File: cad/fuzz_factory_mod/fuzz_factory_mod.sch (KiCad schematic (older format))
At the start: 2 parts

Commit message: Continued schematic.
Modified fuuz_factory circuit : use of matched transistor pairs.
Added USB interface, through FT230X and direct to MCU.
Associated footprints, except for XTAL and trimmers.
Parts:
- NT101, NT102: renamed from NT?; footprint (none) -> Oddities:NetTie-II
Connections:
- net labels added: +3.3V
- net labels removed: +7.5V
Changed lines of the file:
@@
 $Descr A4 11693 8268
 encoding utf-8
-Sheet 1 19
+Sheet 1 22
 Title ""
 Date ""
@@
 $EndSheet
 $Comp
-L power:GNDA #PWR?
+L power:GNDA #PWR0106
 U 1 1 5E05A512
 P 9000 6000
-F 0 "#PWR?" H 9000 5750 50  0001 C CNN
+F 0 "#PWR0106" H 9000 5750 50  0001 C CNN
 F 1 "GNDA" H 9005 5827 50  0000 C CNN
 F 2 "" H 9000 6000 50  0001 C CNN
@@
 $EndComp
 $Comp
-L power:GNDPWR #PWR?
+L power:GNDPWR #PWR0107
 U 1 1 5E05AF8B
 P 9500 6000
-F 0 "#PWR?" H 9500 5800 50  0001 C CNN
+F 0 "#PWR0107" H 9500 5800 50  0001 C CNN
 F 1 "GNDPWR" H 9504 5846 50  0000 C CNN
 F 2 "" H 9500 5950 50  0001 C CNN
@@
 $EndComp
 $Comp
-L power:GNDD #PWR?
+L power:GNDD #PWR0108
 U 1 1 5E05B768
 P 10000 6000
-F 0 "#PWR?" H 10000 5750 50  0001 C CNN
+F 0 "#PWR0108" H 10000 5750 50  0001 C CNN
 F 1 "GNDD" H 10004 5845 50  0000 C CNN
 F 2 "" H 10000 6000 50  0001 C CNN
@@
 $EndComp
 $Comp
-L Device:Net-Tie_2 NT?
+L Device:Net-Tie_2 NT101
 U 1 1 5E05BC9C
 P 9250 5800
-F 0 "NT?" H 9250 5981 50  0000 C CNN
+F 0 "NT101" H 9250 5981 50  0000 C CNN
 F 1 "Net-Tie_2" H 9250 5890 50  0000 C CNN
-F 2 "" H 9250 5800 50  0001 C CNN
+F 2 "Oddities:NetTie-II" H 9250 5800 50  0001 C CNN
 F 3 "~" H 9250 5800 50  0001 C CNN
 	1    9250 5800
@@
 $EndComp
 $Comp
-L Device:Net-Tie_2 NT?
+L Device:Net-Tie_2 NT102
 U 1 1 5E05C2E4
 P 9750 5800
-F 0 "NT?" H 9750 5981 50  0000 C CNN
+F 0 "NT102" H 9750 5981 50  0000 C CNN
 F 1 "Net-Tie_2" H 9750 5890 50  0000 C CNN
-F 2 "" H 9750 5800 50  0001 C CNN
+F 2 "Oddities:NetTie-II" H 9750 5800 50  0001 C CNN
 F 3 "~" H 9750 5800 50  0001 C CNN
 	1    9750 5800
@@
 F4 "VCOM" I R 2000 6900 50
 F5 "GND_ANALOG" I L 1000 7100 50
-F6 "7V_OUT" I R 2000 6800 50
-$EndSheet
-$Comp
-L power:VCOM #PWR?
+F6 "3V3_OUT" I R 2000 6800 50
+$EndSheet
+$Comp
+L power:VCOM #PWR0105
 U 1 1 5E32D8FB
 P 2300 6700
-F 0 "#PWR?" H 2300 6550 50  0001 C CNN
+F 0 "#PWR0105" H 2300 6550 50  0001 C CNN
 F 1 "VCOM" V 2300 6950 50  0000 C CNN
 F 2 "" H 2300 6700 50  0001 C CNN
@@
 	2300 6900 2300 6700
 $Comp
-L power:GNDD #PWR?
+L power:GNDD #PWR0101
 U 1 1 5E32E854
 P 700 7200
-F 0 "#PWR?" H 700 6950 50  0001 C CNN
+F 0 "#PWR0101" H 700 6950 50  0001 C CNN
 F 1 "GNDD" H 704 7045 50  0000 C CNN
 F 2 "" H 700 7200 50  0001 C CNN
@@
 $EndComp
 $Comp
-L power:GNDA #PWR?
+L power:GNDA #PWR0103
 U 1 1 5E330132
 P 900 7200
-F 0 "#PWR?" H 900 6950 50  0001 C CNN
+F 0 "#PWR0103" H 900 6950 50  0001 C CNN
 F 1 "GNDA" H 905 7027 50  0000 C CNN
 F 2 "" H 900 7200 50  0001 C CNN
@@
 	700  7000 700  7200
 $Comp
-L power:+BATT #PWR?
+L power:+BATT #PWR0102
 U 1 1 5E3312DB
 P 900 6700
-F 0 "#PWR?" H 900 6550 50  0001 C CNN
+F 0 "#PWR0102" H 900 6550 50  0001 C CNN
 F 1 "+BATT" H 915 6873 50  0000 C CNN
 F 2 "" H 900 6700 50  0001 C CNN
@@
 Wire Wire Line
 	900  6800 1000 6800
-$Comp
-L power:+7.5V #PWR?
-U 1 1 5E6791DE
-P 2100 6700
-F 0 "#PWR?" H 2100 6550 50  0001 C CNN
-F 1 "+7.5V" H 2115 6873 50  0000 C CNN
-F 2 "" H 2100 6700 50  0001 C CNN
-F 3 "" H 2100 6700 50  0001 C CNN
-	1    2100 6700
-	1    0    0    -1
-$EndComp
 $Sheet
 S 1000 4500 1000 500
@@
 F3 "MIDI_OUT" I R 2000 4900 50
 $EndSheet
+$Comp
+L power:+3.3V #PWR0104
+U 1 1 5E936014
+P 2100 6700
+F 0 "#PWR0104" H 2100 6550 50  0001 C CNN
+F 1 "+3.3V" H 2115 6873 50  0000 C CNN
+F 2 "" H 2100 6700 50  0001 C CNN
+F 3 "" H 2100 6700 50  0001 C CNN
+	1    2100 6700
+	1    0    0    -1
+$EndComp
 $EndSCHEMATC

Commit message: Continued schematic.
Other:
- moved on the sheet: NT101, NT102
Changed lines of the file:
@@
 $Descr A4 11693 8268
 encoding utf-8
-Sheet 1 22
+Sheet 1 26
 Title ""
 Date ""
@@
 $EndDescr
 $Sheet
-S 2000 1000 1500 1000
+S 3000 1000 1000 1500
 U 5DE4AD26
 F0 "MCU" 50
@@
 $EndSheet
 $Sheet
-S 5000 1000 1000 2500
+S 10000 1000 1000 2500
 U 5DE4AD88
 F0 "ANALOG" 50
 F1 "analog.sch" 50
-F2 "GAIN_POT_1" I L 5000 1700 50
-F3 "GAIN_POT_2" I L 5000 1800 50
-F4 "GAIN_POT_3" I L 5000 1900 50
-F5 "COMP_POT_1" I L 5000 2000 50
-F6 "COMP_POT_2" I L 5000 2100 50
-F7 "VOLUME_POT_1" I L 5000 2200 50
-F8 "VOLUME_POT_2" I L 5000 2300 50
-F9 "VOLUME_POT_3" I L 5000 2400 50
-F10 "GATE_POT_1" I L 5000 2500 50
-F11 "GATE_POT_2" I L 5000 2600 50
-F12 "IN_AUDIO" I L 5000 1600 50
-F13 "IN_PWM_LSB" I L 5000 1100 50
-F14 "IN_PWM_LSBn" I L 5000 1200 50
-F15 "IN_PWM_MSB" I L 5000 1300 50
-F16 "IN_PWM_MSBn" I L 5000 1400 50
-F17 "STARVE_POT_1" I L 5000 2700 50
-F18 "STARVE_POT_2" I L 5000 2800 50
-F19 "OUT_AUDIO" I R 6000 1600 50
-F20 "~DIGIPOT_SHDN" I L 5000 3000 50
-F21 "DIGIPOT_CLK" I L 5000 3100 50
-F22 "DIGIPOT_SDI" I L 5000 3200 50
-F23 "~DIGIPOT_CS" I L 5000 3300 50
-F24 "~DIGIPOT_PR" I L 5000 3400 50
+F2 "GAIN_POT_1" I L 10000 1700 50
+F3 "GAIN_POT_2" I L 10000 1800 50
+F4 "GAIN_POT_3" I L 10000 1900 50
+F5 "COMP_POT_1" I L 10000 2000 50
+F6 "COMP_POT_2" I L 10000 2100 50
+F7 "VOLUME_POT_1" I L 10000 2200 50
+F8 "VOLUME_POT_2" I L 10000 2300 50
+F9 "VOLUME_POT_3" I L 10000 2400 50
+F10 "GATE_POT_1" I L 10000 2500 50
+F11 "GATE_POT_2" I L 10000 2600 50
+F12 "IN_AUDIO" I L 10000 1600 50
+F13 "IN_PWM_LSB" I L 10000 1100 50
+F14 "IN_PWM_LSBn" I L 10000 1200 50
+F15 "IN_PWM_MSB" I L 10000 1300 50
+F16 "IN_PWM_MSBn" I L 10000 1400 50
+F17 "STARVE_POT_1" I L 10000 2700 50
+F18 "STARVE_POT_2" I L 10000 2800 50
+F19 "OUT_AUDIO" I R 11000 1600 50
+F20 "~DIGIPOT_SHDN" I L 10000 3000 50
+F21 "DIGIPOT_CLK" I L 10000 3100 50
+F22 "DIGIPOT_SDI" I L 10000 3200 50
+F23 "~DIGIPOT_CS" I L 10000 3300 50
+F24 "~DIGIPOT_PR" I L 10000 3400 50
 $EndSheet
 $Sheet
@@
 L power:GNDA #PWR0106
 U 1 1 5E05A512
-P 9000 6000
-F 0 "#PWR0106" H 9000 5750 50  0001 C CNN
-F 1 "GNDA" H 9005 5827 50  0000 C CNN
-F 2 "" H 9000 6000 50  0001 C CNN
-F 3 "" H 9000 6000 50  0001 C CNN
-	1    9000 6000
-	1    0    0    -1
-$EndComp
-$Comp
-L power:GNDPWR #PWR0107
-U 1 1 5E05AF8B
-P 9500 6000
-F 0 "#PWR0107" H 9500 5800 50  0001 C CNN
-F 1 "GNDPWR" H 9504 5846 50  0000 C CNN
-F 2 "" H 9500 5950 50  0001 C CNN
-F 3 "" H 9500 5950 50  0001 C CNN
-	1    9500 6000
-	1    0    0    -1
-$EndComp
-$Comp
-L power:GNDD #PWR0108
-U 1 1 5E05B768
 P 10000 6000
-F 0 "#PWR0108" H 10000 5750 50  0001 C CNN
-F 1 "GNDD" H 10004 5845 50  0000 C CNN
+F 0 "#PWR0106" H 10000 5750 50  0001 C CNN
+F 1 "GNDA" H 10005 5827 50  0000 C CNN
 F 2 "" H 10000 6000 50  0001 C CNN
 F 3 "" H 10000 6000 50  0001 C CNN
@@
 $EndComp
 $Comp
+L power:GNDPWR #PWR0107
+U 1 1 5E05AF8B
+P 10500 6000
+F 0 "#PWR0107" H 10500 5800 50  0001 C CNN
+F 1 "GNDPWR" H 10504 5846 50  0000 C CNN
+F 2 "" H 10500 5950 50  0001 C CNN
+F 3 "" H 10500 5950 50  0001 C CNN
+	1    10500 6000
+	1    0    0    -1
+$EndComp
+$Comp
+L power:GNDD #PWR0108
+U 1 1 5E05B768
+P 11000 6000
+F 0 "#PWR0108" H 11000 5750 50  0001 C CNN
+F 1 "GNDD" H 11004 5845 50  0000 C CNN
+F 2 "" H 11000 6000 50  0001 C CNN
+F 3 "" H 11000 6000 50  0001 C CNN
+	1    11000 6000
+	1    0    0    -1
+$EndComp
+$Comp
 L Device:Net-Tie_2 NT101
 U 1 1 5E05BC9C
-P 9250 5800
-F 0 "NT101" H 9250 5981 50  0000 C CNN
-F 1 "Net-Tie_2" H 9250 5890 50  0000 C CNN
-F 2 "Oddities:NetTie-II" H 9250 5800 50  0001 C CNN
-F 3 "~" H 9250 5800 50  0001 C CNN
-	1    9250 5800
+P 10250 5800
+F 0 "NT101" H 10250 5981 50  0000 C CNN
+F 1 "Net-Tie_2" H 10250 5890 50  0000 C CNN
+F 2 "Oddities:NetTie-II" H 10250 5800 50  0001 C CNN
+F 3 "~" H 10250 5800 50  0001 C CNN
+	1    10250 5800
 	1    0    0    -1
 $EndComp
@@
 L Device:Net-Tie_2 NT102
 U 1 1 5E05C2E4
-P 9750 5800
-F 0 "NT102" H 9750 5981 50  0000 C CNN
-F 1 "Net-Tie_2" H 9750 5890 50  0000 C CNN
-F 2 "Oddities:NetTie-II" H 9750 5800 50  0001 C CNN
-F 3 "~" H 9750 5800 50  0001 C CNN
-	1    9750 5800
+P 10750 5800
+F 0 "NT102" H 10750 5981 50  0000 C CNN
+F 1 "Net-Tie_2" H 10750 5890 50  0000 C CNN
+F 2 "Oddities:NetTie-II" H 10750 5800 50  0001 C CNN
+F 3 "~" H 10750 5800 50  0001 C CNN
+	1    10750 5800
 	1    0    0    -1
 $EndComp
 Wire Wire Line
+	11000 6000 11000 5800
+Wire Wire Line
+	11000 5800 10850 5800
+Wire Wire Line
+	10650 5800 10500 5800
+Wire Wire Line
+	10500 6000 10500 5800
+Connection ~ 10500 5800
+Wire Wire Line
+	10500 5800 10350 5800
+Wire Wire Line
 	10000 6000 10000 5800
 Wire Wire Line
-	10000 5800 9850 5800
-Wire Wire Line
-	9650 5800 9500 5800
-Wire Wire Line
-	9500 6000 9500 5800
-Connection ~ 9500 5800
-Wire Wire Line
-	9500 5800 9350 5800
-Wire Wire Line
-	9000 6000 9000 5800
-Wire Wire Line
-	9000 5800 9150 5800
-$Sheet
-S 9500 800  1500 2100
-U 5E083283
-F0 "Interface" 50
-F1 "interface01.sch" 50
-F2 "DISP_CLK" I L 9500 1300 50
-F3 "DISP_DATA" I L 9500 1400 50
-F4 "DISP_ENABLE" I L 9500 1500 50
-F5 "DISP_LATCH" I L 9500 1600 50
-F6 "ENC1_SW" I L 9500 1800 50
-F7 "ENC1_LED1" I L 9500 1900 50
-F8 "ENC1_LED2" I L 9500 2000 50
-F9 "ENC1_ENC1" I R 11000 1900 50
-F10 "ENC1_ENC2" I R 11000 2000 50
-F11 "FSW_bypass" I L 9500 1100 50
-F12 "ENC2_SW" I L 9500 2200 50
-F13 "ENC2_LED1" I L 9500 2300 50
-F14 "ENC2_LED2" I L 9500 2400 50
-F15 "ENC2_ENC1" I R 11000 2300 50
-F16 "ENC2_ENC2" I R 11000 2400 50
-F17 "ENC3_SW" I L 9500 2600 50
-F18 "ENC3_LED1" I L 9500 2700 50
-F19 "ENC3_LED2" I L 9500 2800 50
-F20 "ENC3_ENC1" I R 11000 2700 50
-F21 "ENC3_ENC2" I R 11000 2800 50
-$EndSheet
+	10000 5800 10150 5800
 $Sheet
 S 1000 6700 1000 500

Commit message: Continued schematic.
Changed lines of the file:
@@
 $Descr A4 11693 8268
 encoding utf-8
-Sheet 1 26
+Sheet 1 30
 Title ""
 Date ""
@@
 Wire Wire Line
 	900  6800 1000 6800
-$Sheet
-S 1000 4500 1000 500
-U 5E67C282
-F0 "MIDI" 50
-F1 "MIDI.sch" 50
-F2 "MIDI_IN" I R 2000 4600 50
-F3 "MIDI_OUT" I R 2000 4900 50
-$EndSheet
 $Comp
 L power:+3.3V #PWR0104
@@
 	1    0    0    -1
 $EndComp
+Text GLabel 3900 6900 0    50   Input ~ 0
+BYPASS_CMD
+Wire Wire Line
+	4000 6900 3900 6900
 $EndSCHEMATC

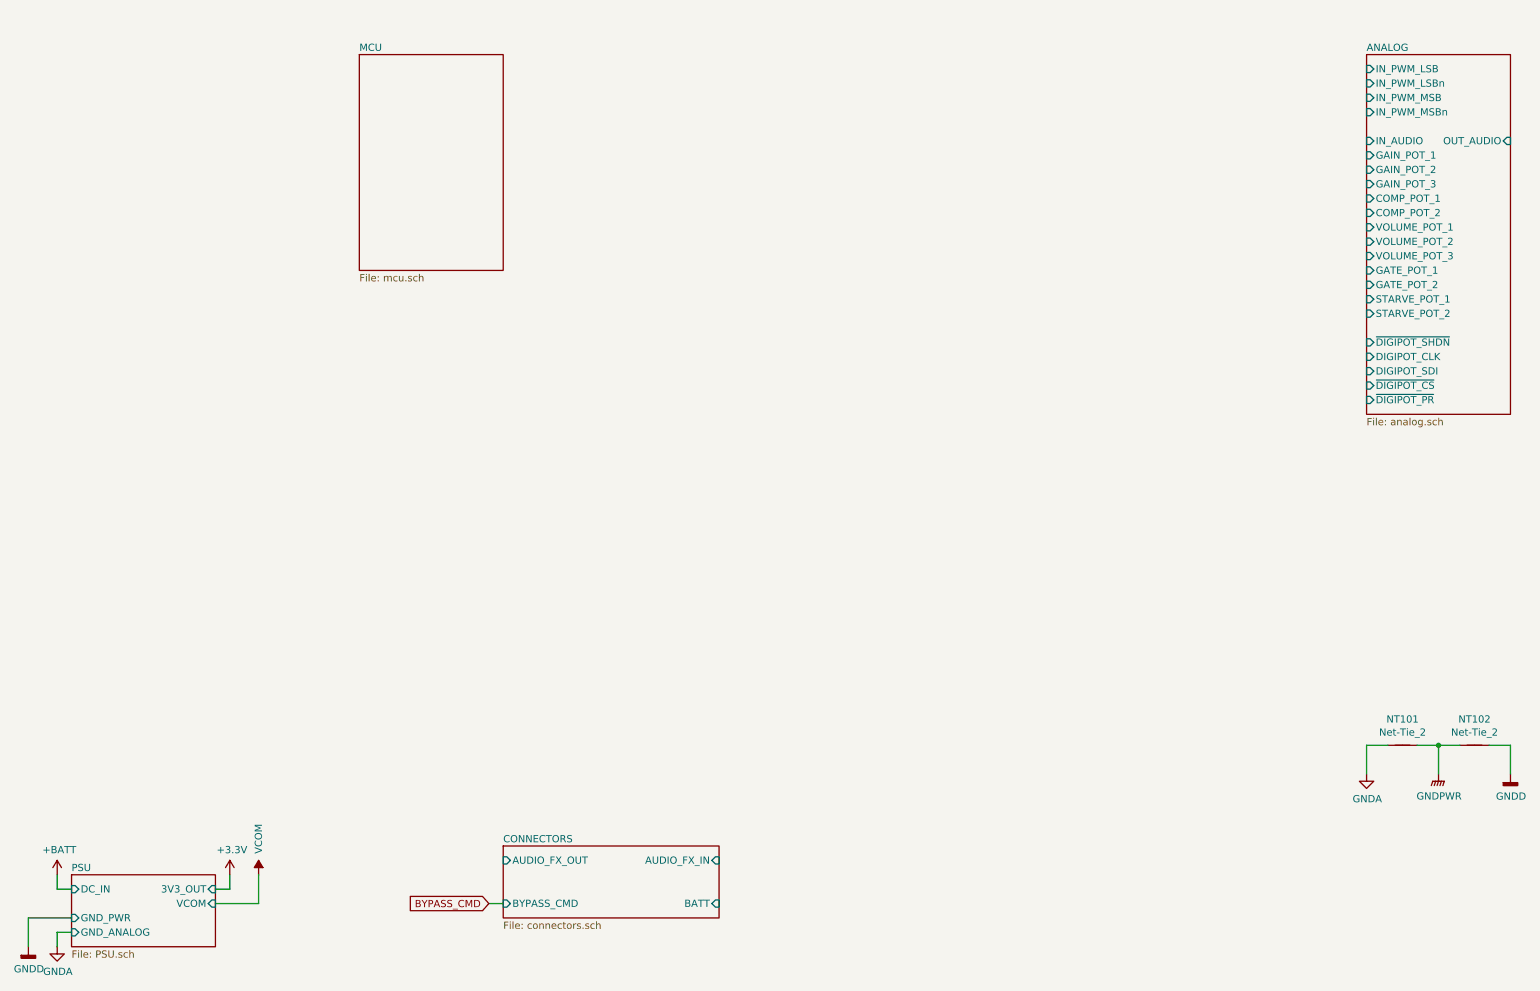
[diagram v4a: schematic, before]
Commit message: Continued schematic.
Continued component placement.
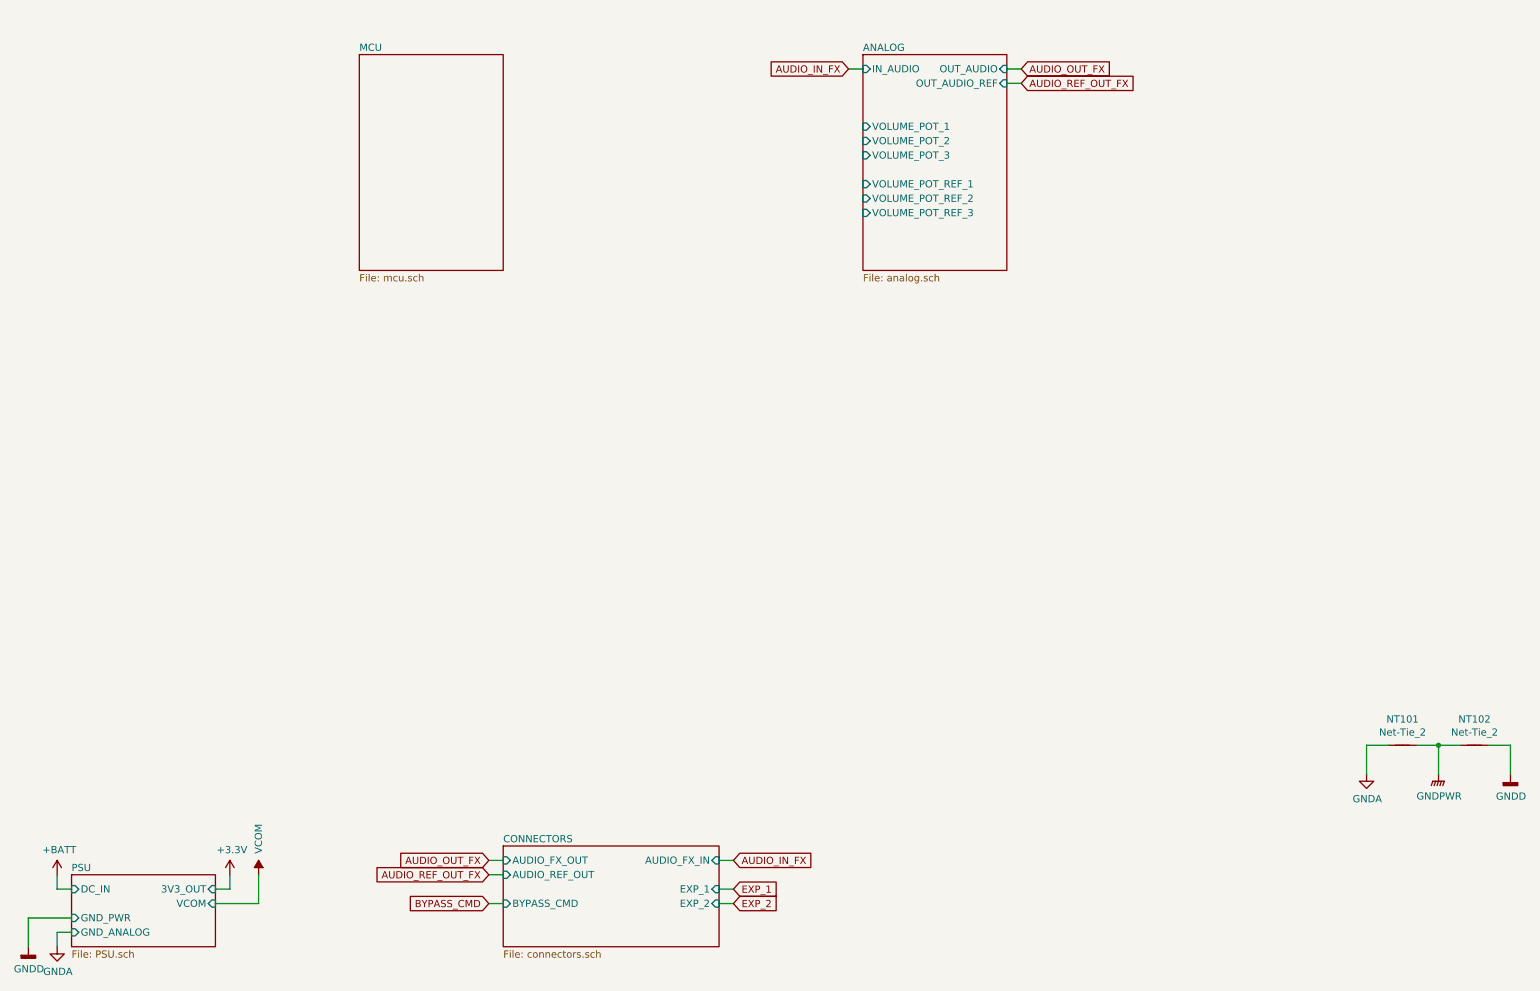
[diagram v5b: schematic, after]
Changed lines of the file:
@@
 $EndSheet
 $Sheet
-S 10000 1000 1000 2500
+S 6500 1000 1000 1500
 U 5DE4AD88
 F0 "ANALOG" 50
 F1 "analog.sch" 50
-F2 "GAIN_POT_1" I L 10000 1700 50
-F3 "GAIN_POT_2" I L 10000 1800 50
-F4 "GAIN_POT_3" I L 10000 1900 50
-F5 "COMP_POT_1" I L 10000 2000 50
-F6 "COMP_POT_2" I L 10000 2100 50
-F7 "VOLUME_POT_1" I L 10000 2200 50
-F8 "VOLUME_POT_2" I L 10000 2300 50
-F9 "VOLUME_POT_3" I L 10000 2400 50
-F10 "GATE_POT_1" I L 10000 2500 50
-F11 "GATE_POT_2" I L 10000 2600 50
-F12 "IN_AUDIO" I L 10000 1600 50
-F13 "IN_PWM_LSB" I L 10000 1100 50
-F14 "IN_PWM_LSBn" I L 10000 1200 50
-F15 "IN_PWM_MSB" I L 10000 1300 50
-F16 "IN_PWM_MSBn" I L 10000 1400 50
-F17 "STARVE_POT_1" I L 10000 2700 50
-F18 "STARVE_POT_2" I L 10000 2800 50
-F19 "OUT_AUDIO" I R 11000 1600 50
-F20 "~DIGIPOT_SHDN" I L 10000 3000 50
-F21 "DIGIPOT_CLK" I L 10000 3100 50
-F22 "DIGIPOT_SDI" I L 10000 3200 50
-F23 "~DIGIPOT_CS" I L 10000 3300 50
-F24 "~DIGIPOT_PR" I L 10000 3400 50
+F2 "VOLUME_POT_1" I L 6500 1500 50
+F3 "VOLUME_POT_2" I L 6500 1600 50
+F4 "VOLUME_POT_3" I L 6500 1700 50
+F5 "IN_AUDIO" I L 6500 1100 50
+F6 "OUT_AUDIO" I R 7500 1100 50
+F7 "OUT_AUDIO_REF" I R 7500 1200 50
+F8 "VOLUME_POT_REF_1" I L 6500 1900 50
+F9 "VOLUME_POT_REF_2" I L 6500 2000 50
+F10 "VOLUME_POT_REF_3" I L 6500 2100 50
 $EndSheet
 $Sheet
-S 4000 6500 1500 500
+S 4000 6500 1500 700
 U 5DE5A177
 F0 "CONNECTORS" 50
@@
 F3 "AUDIO_FX_IN" I R 5500 6600 50
 F4 "AUDIO_FX_OUT" I L 4000 6600 50
-F5 "BATT" I R 5500 6900 50
+F5 "EXP_1" I R 5500 6800 50
+F6 "EXP_2" I R 5500 6900 50
+F7 "AUDIO_REF_OUT" I L 4000 6700 50
 $EndSheet
 $Comp
@@
 Wire Wire Line
 	4000 6900 3900 6900
+Text GLabel 5600 6600 2    50   Input ~ 0
+AUDIO_IN_FX
+Text GLabel 3900 6600 0    50   Input ~ 0
+AUDIO_OUT_FX
+Wire Wire Line
+	3900 6600 4000 6600
+Wire Wire Line
+	5500 6600 5600 6600
+Text GLabel 6400 1100 0    50   Input ~ 0
+AUDIO_IN_FX
+Wire Wire Line
+	6500 1100 6400 1100
+Text GLabel 7600 1100 2    50   Input ~ 0
+AUDIO_OUT_FX
+Wire Wire Line
+	7600 1100 7500 1100
+Text GLabel 5600 6800 2    50   Input ~ 0
+EXP_1
+Text GLabel 5600 6900 2    50   Input ~ 0
+EXP_2
+Wire Wire Line
+	5500 6800 5600 6800
+Wire Wire Line
+	5600 6900 5500 6900
+Text GLabel 3900 6700 0    50   Input ~ 0
+AUDIO_REF_OUT_FX
+Wire Wire Line
+	4000 6700 3900 6700
+Text GLabel 7600 1200 2    50   Input ~ 0
+AUDIO_REF_OUT_FX
+Wire Wire Line
+	7600 1200 7500 1200
 $EndSCHEMATC
